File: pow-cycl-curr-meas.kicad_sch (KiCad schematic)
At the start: 62 parts, among them Q1 SQS401EN-T1_BE3, Q10 2N7002, Q2 SQS401EN-T1_BE3, Q3 2N7002, Q4 2N7002, Q5 SQS401EN-T1_BE3, Q6 2N7002, Q7 SQS401EN-T1_BE3, Q8 SQS401EN-T1_BE3, Q9 2N7002, U10 TCA9534, U11 TMCS1100A2-Q1, U12 TMCS1100A2-Q1, U13 TMCS1100A2-Q1, U14 ADS7828, U8 TMCS1100A2-Q1, U9 TMCS1100A2-Q1

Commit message: Loclib
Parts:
- Q10, Q3, Q4, Q6, Q9: footprint antmicro-footprints:SOT-23-3 -> nuc-compute-cluster-power-breakout-footprints:SOT-23-3; symbol antmicroTransistorsFETsMOSFETsSingle:2N7002 -> nuc-compute-cluster-power-breakout:2N7002

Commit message: Update README
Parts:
- C21, C28, C29, C30, C31, C32, C37: footprint nuc-compute-cluster-power-breakout-footprints:0402-cap -> d1600e-psu-breakout-board-footprints:0402-cap; symbol nuc-compute-cluster-power-breakout:C_100n_0402 -> d1600e-psu-breakout-board:C_100n_0402
- C22: footprint nuc-compute-cluster-power-breakout-footprints:0402-cap -> d1600e-psu-breakout-board-footprints:0402-cap; symbol nuc-compute-cluster-power-breakout:C_1u_0402 -> d1600e-psu-breakout-board:C_1u_0402
- FB4: footprint nuc-compute-cluster-power-breakout-footprints:0603 -> d1600e-psu-breakout-board-footprints:0603; symbol nuc-compute-cluster-power-breakout:BLM18AG601SN1D -> d1600e-psu-breakout-board:BLM18AG601SN1D
- Q1, Q2, Q5, Q7, Q8: footprint nuc-compute-cluster-power-breakout-footprints:Vishay_PowerPAK_1212-8_Single -> d1600e-psu-breakout-board-footprints:Vishay_PowerPAK_1212-8_Single; symbol nuc-compute-cluster-power-breakout:SQS401EN-T1_BE3 -> d1600e-psu-breakout-board:SQS401EN-T1_BE3
- Q10, Q3, Q4, Q6, Q9: footprint nuc-compute-cluster-power-breakout-footprints:SOT-23-3 -> d1600e-psu-breakout-board-footprints:SOT-23-3; symbol nuc-compute-cluster-power-breakout:2N7002 -> d1600e-psu-breakout-board:2N7002
- R13, R14, R15, R16, R17, R18, R30, R31, R32, R33: footprint nuc-compute-cluster-power-breakout-footprints:0402-res -> d1600e-psu-breakout-board-footprints:0402-res; symbol nuc-compute-cluster-power-breakout:R_0R_0402 -> d1600e-psu-breakout-board:R_0R_0402
- R19, R22, R23, R25, R28, R29: footprint nuc-compute-cluster-power-breakout-footprints:0402-res -> d1600e-psu-breakout-board-footprints:0402-res; symbol nuc-compute-cluster-power-breakout:R_4k7_0402 -> d1600e-psu-breakout-board:R_4k7_0402
- R20, R21, R24, R26, R27, R46, R47, R48, R49, R50: footprint nuc-compute-cluster-power-breakout-footprints:0402-res -> d1600e-psu-breakout-board-footprints:0402-res; symbol nuc-compute-cluster-power-breakout:R_10k_0402 -> d1600e-psu-breakout-board:R_10k_0402
- TP_ADC1, TP_ADC2, TP_ADC3, TP_ADC4, TP_ADC5, TP_PC1, TP_PC2, TP_PC3, TP_PC4, TP_PC5: footprint nuc-compute-cluster-power-breakout-footprints:Testpoint_smd_1mm -> d1600e-psu-breakout-board-footprints:Testpoint_smd_1mm; symbol nuc-compute-cluster-power-breakout:TP_SMD1MM -> d1600e-psu-breakout-board:TP_SMD1MM
- U10: footprint nuc-compute-cluster-power-breakout-footprints:TSSOP-16 -> d1600e-psu-breakout-board-footprints:TSSOP-16; symbol nuc-compute-cluster-power-breakout:TCA9534 -> d1600e-psu-breakout-board:TCA9534
- U11, U12, U13, U8, U9: footprint nuc-compute-cluster-power-breakout-footprints:SOIC-8_W3.9mm -> d1600e-psu-breakout-board-footprints:SOIC-8_W3.9mm; symbol nuc-compute-cluster-power-breakout:TMCS1100A2-Q1 -> d1600e-psu-breakout-board:TMCS1100A2-Q1
- U14: footprint nuc-compute-cluster-power-breakout-footprints:TSSOP-16_4.4x5mm_P0.65mm -> d1600e-psu-breakout-board-footprints:TSSOP-16_4.4x5mm_P0.65mm; symbol nuc-compute-cluster-power-breakout:ADS7828 -> d1600e-psu-breakout-board:ADS7828
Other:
- company: Antmicro LTD -> (none)
- title: NUC Computer Cluster Power Breakout HW -> D1600E PSU Breakout Board

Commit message: Added some changes after 1st review
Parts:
- removed Q1, Q2, Q5, Q7, Q8: SQS401EN-T1_BE3, d1600e-psu-breakout-board-footprints:Vishay_PowerPAK_1212-8_Single, symbol d1600e-psu-breakout-board:SQS401EN-T1_BE3
- added QA1, QA2, QA3, QA4, QA5, QB1, QB2, QB3, QB4, QB5: SI7613DN-T1-GE3, antmicro-footprints:Vishay_PowerPAK_1212-8_Single, symbol antmicroTransistorsFETsMOSFETsSingle:SI7613DN-T1-GE3
- renumbered Q6 to Q10, Q3 to Q6, Q4 to Q7, Q10 to Q8
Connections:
- net C_MEAS_1: now also QA1.5 (D), QB1.5 (D)
- net C_MEAS_2: now also QA2.5 (D), QB2.5 (D)
- net C_MEAS_3: now also QA3.5 (D), QB3.5 (D)
- net C_MEAS_4: now also QA4.5 (D), QB4.5 (D)
- net C_MEAS_5: now also QA5.5 (D), QB5.5 (D)
- net VCC12V0: now also QA1.1 (S), QA1.2 (S), QA1.3 (S), QA2.1 (S), QA2.2 (S), QA2.3 (S), QA3.1 (S), QA3.2 (S), QA3.3 (S), QA4.1 (S), QA4.2 (S), QA4.3 (S), QA5.1 (S), QA5.2 (S), QA5.3 (S), QB1.1 (S), QB1.2 (S), QB1.3 (S), QB2.1 (S), QB2.2 (S), QB2.3 (S), QB3.1 (S), QB3.2 (S), QB3.3 (S), QB4.1 (S), QB4.2 (S), QB4.3 (S), QB5.1 (S), QB5.2 (S), QB5.3 (S)
- net at Q6.3 (D), R22.2: now also QA1.4 (G), QB1.4 (G)
- net at Q10.3 (D), R25.2: now also QA5.4 (G), QB5.4 (G)
- net at Q7.3 (D), R23.2: now also QA2.4 (G), QB2.4 (G)
- net at Q8.3 (D), R29.2: now also QA3.4 (G), QB3.4 (G)
- net at Q9.3 (D), R28.2: now also QA4.4 (G), QB4.4 (G)

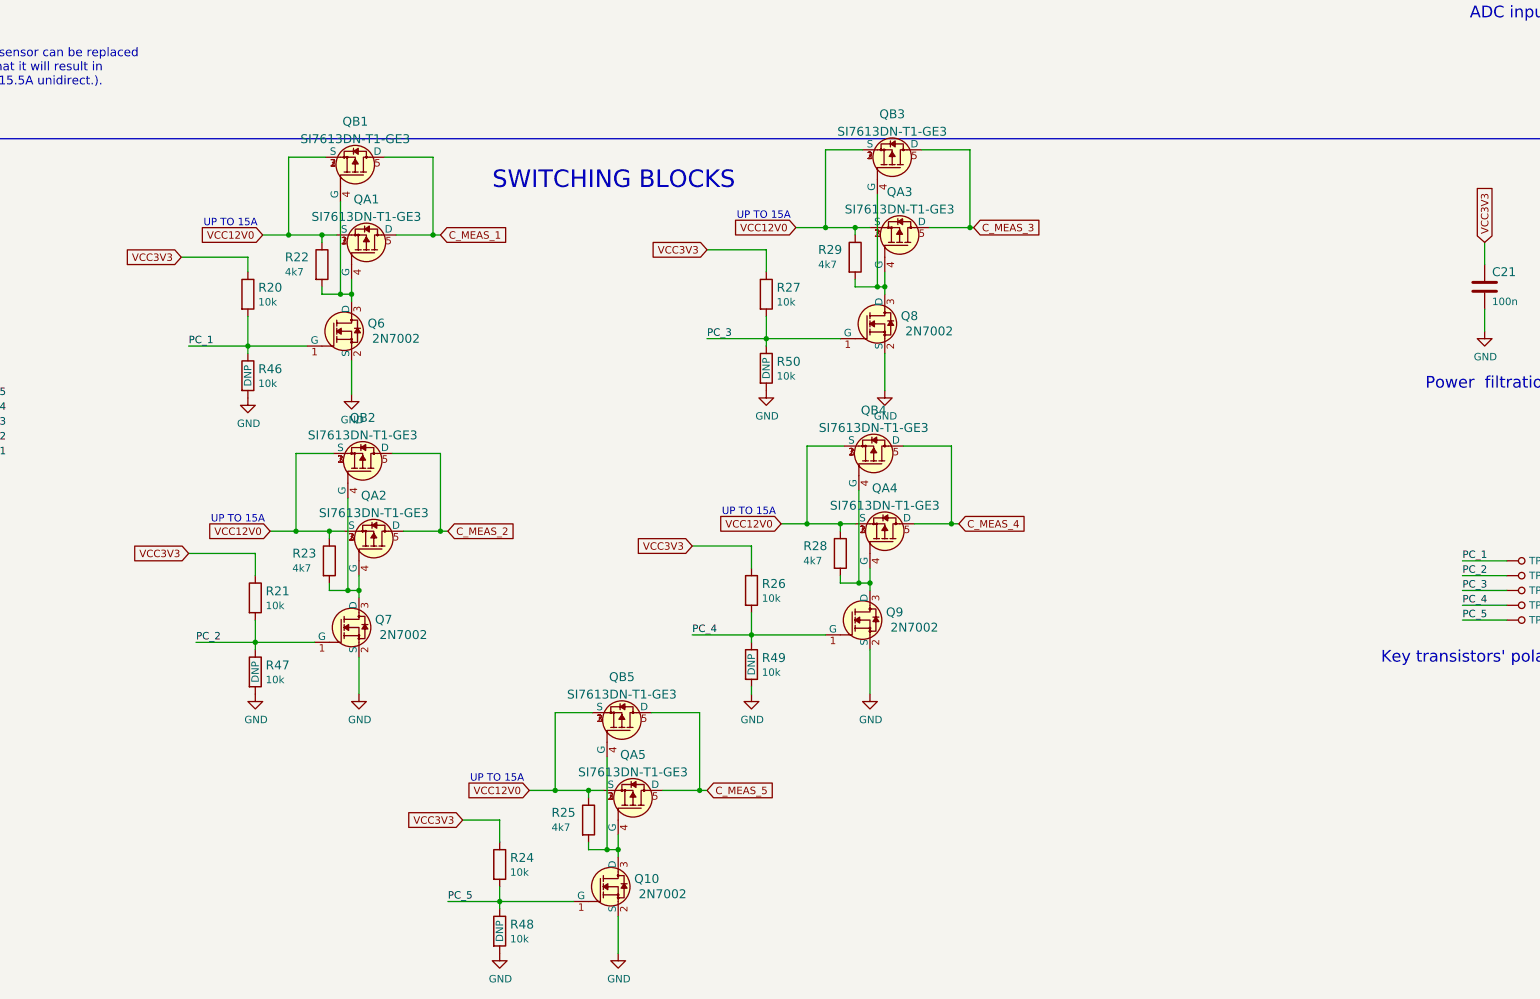
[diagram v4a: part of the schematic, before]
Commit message: Added all changes proposed in first review of the board
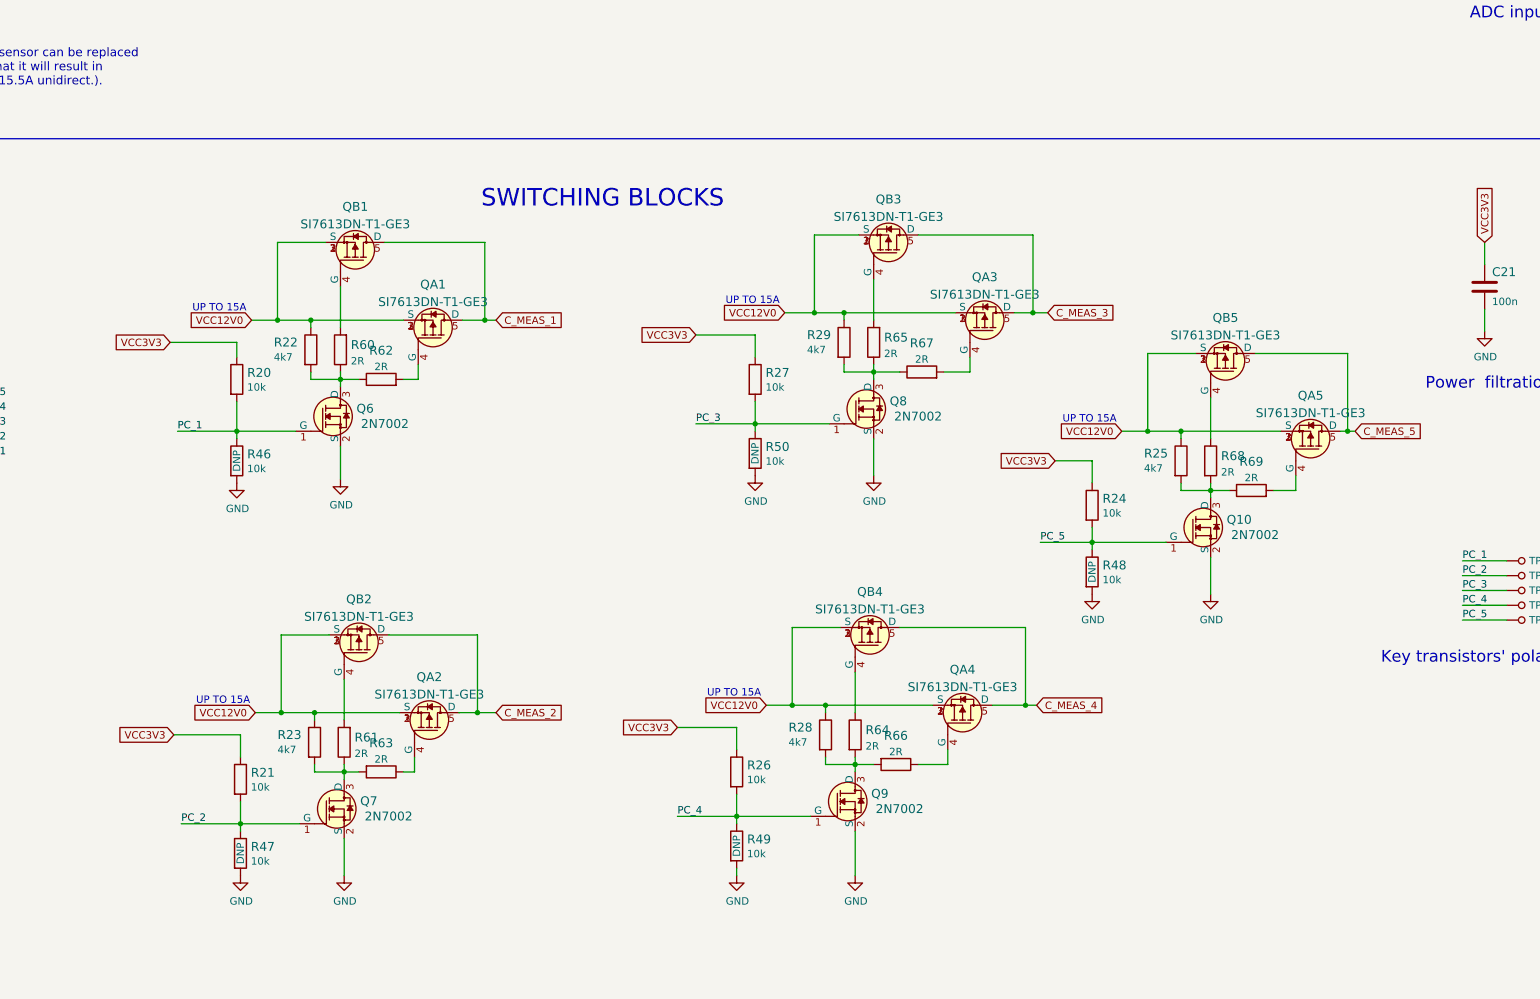
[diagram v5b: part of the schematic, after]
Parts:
- added R60, R61, R62, R63, R64, R65, R66, R67, R68, R69: R_2R_0402, antmicro-footprints:0402-res, symbol antmicroResistors0402:R_2R_0402
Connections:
- net at Q6.3 (D), R22.2: now also R60.1, R62.1; no longer QA1.4 (G), QB1.4 (G)
- net at Q10.3 (D), R25.2: now also R68.2, R69.1; no longer QA5.4 (G), QB5.4 (G)
- net at Q7.3 (D), R23.2: now also R61.1, R63.2; no longer QA2.4 (G), QB2.4 (G)
- net at Q8.3 (D), R29.2: now also R65.1, R67.1; no longer QA3.4 (G), QB3.4 (G)
- net at Q9.3 (D), R28.2: now also R64.2, R66.2; no longer QA4.4 (G), QB4.4 (G)
- new net: QB2.4 (G), R61.2
- new net: QB1.4 (G), R60.2
- new net: QB4.4 (G), R64.1
- new net: QB3.4 (G), R65.2
- new net: QA5.4 (G), R69.2
- new net: QA1.4 (G), R62.2
- new net: QA3.4 (G), R67.2
- new net: QA2.4 (G), R63.1
- new net: QB5.4 (G), R68.1
- new net: QA4.4 (G), R66.1
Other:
- moved on the sheet: Q10, Q6, Q7, Q8, Q9, QA1, QA2, QA3, QA4, QA5, QB1, QB2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

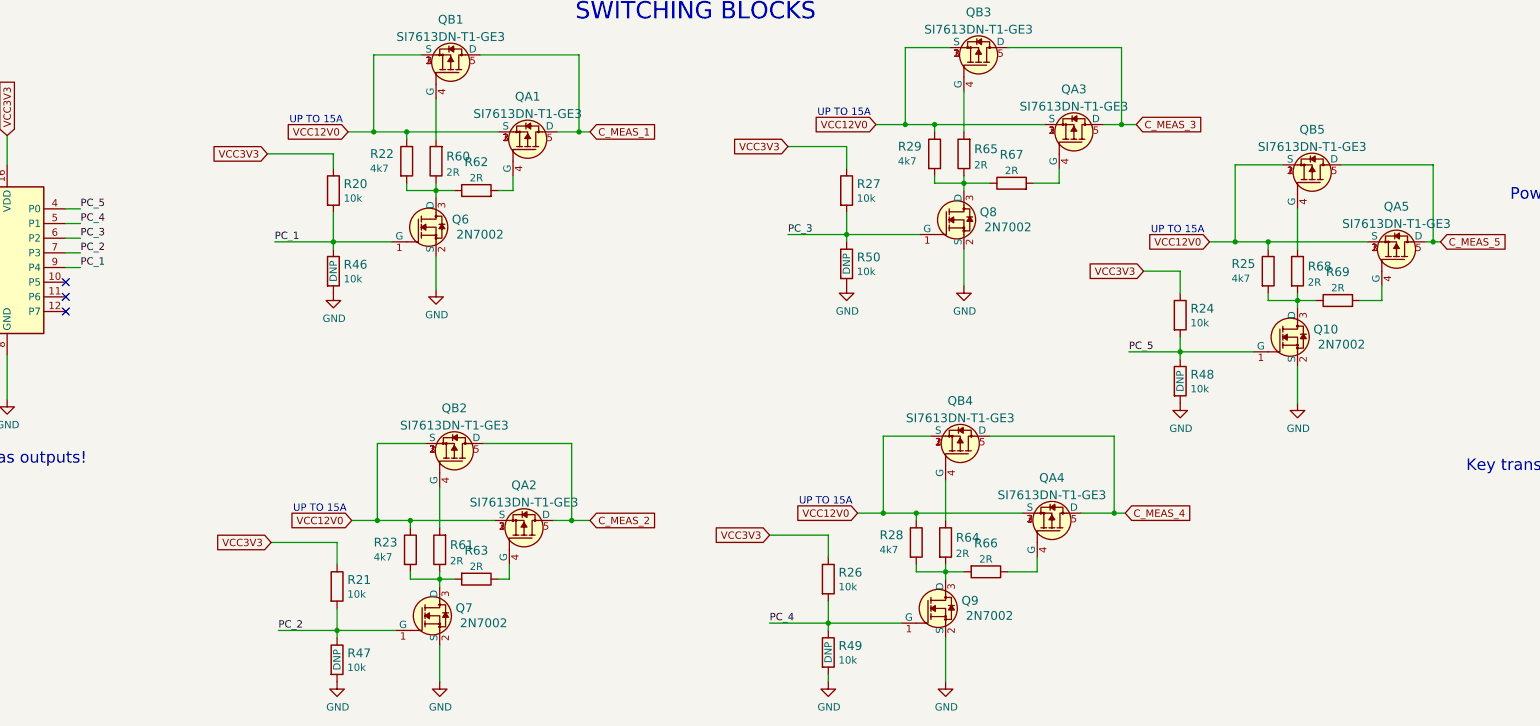
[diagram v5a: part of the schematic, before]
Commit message: Fixed USB tracks,VBUS&GNDD, DRC errors and warning, added protection zener diodes
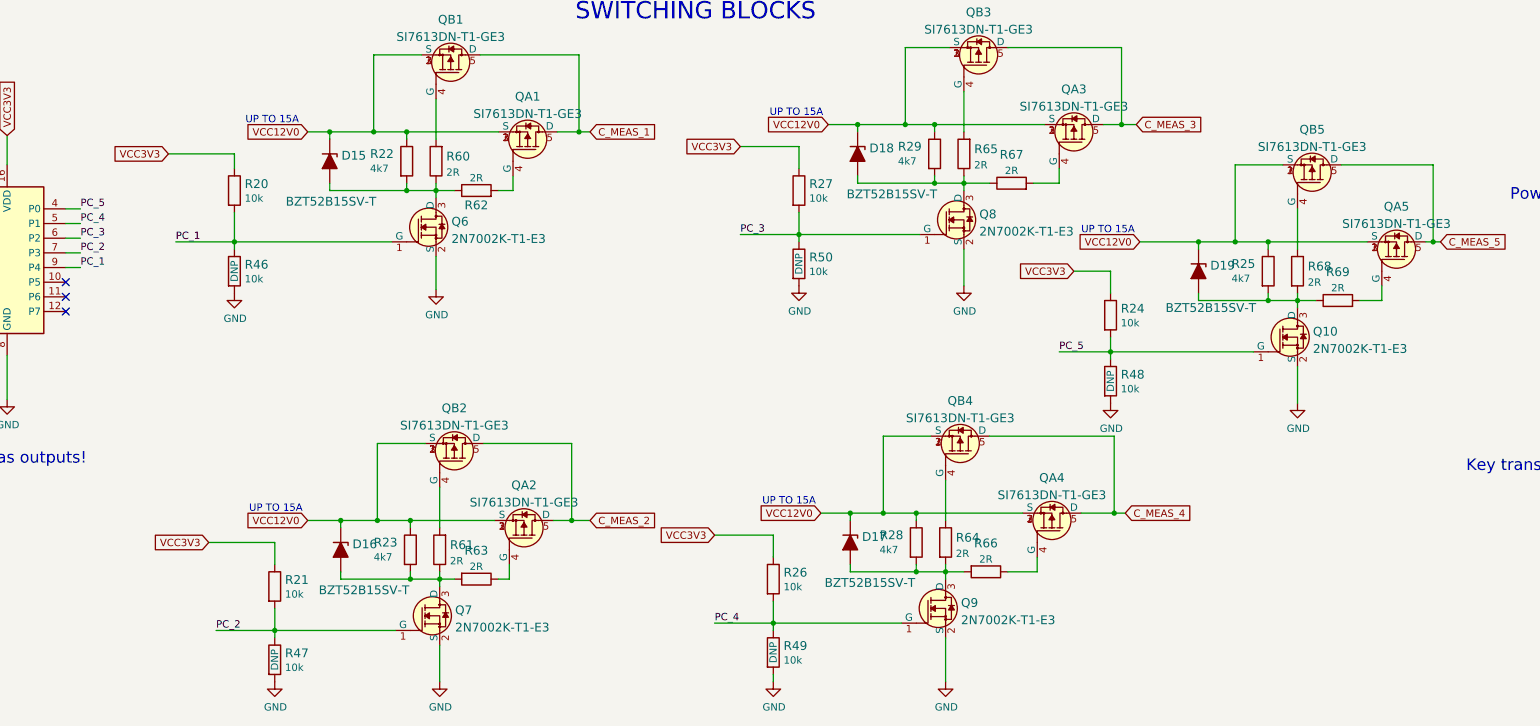
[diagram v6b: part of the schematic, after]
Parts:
- removed Q10, Q6, Q7, Q8, Q9: 2N7002, d1600e-psu-breakout-board-footprints:SOT-23-3, symbol d1600e-psu-breakout-board:2N7002
- added D15, D16, D17, D18, D19: BZT52B15SV-T, antmicro-footprints:SOD-323, symbol antmicroDiodesZenerSingle:BZT52B15SV-T
- added Q10, Q6, Q7, Q8, Q9: 2N7002K-T1-E3, antmicro-footprints:SOT-23-3, symbol antmicroTransistorsFETsMOSFETsSingle:2N7002K-T1-E3
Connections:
- net GND: now also Q10.2 (S), Q6.2 (S), Q7.2 (S), Q8.2 (S), Q9.2 (S)
- net PC_1: now also Q6.1 (G)
- net PC_2: now also Q7.1 (G)
- net PC_3: now also Q8.1 (G)
- net PC_4: now also Q9.1 (G)
- net PC_5: now also Q10.1 (G)
- net VCC12V0: now also D15.K, D16.K, D17.K, D18.K, D19.K
- net at R22.2, R60.1, R62.1: now also D15.A, Q6.3 (D)
- net at R25.2, R68.2, R69.1: now also D19.A, Q10.3 (D)
- net at R23.2, R61.1, R63.2: now also D16.A, Q7.3 (D)
- net at R29.2, R65.1, R67.1: now also D18.A, Q8.3 (D)
- net at R28.2, R64.2, R66.2: now also D17.A, Q9.3 (D)
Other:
- moved on the sheet: R20, R21, R24, R26, R27, R46, R47, R48, R49, R50
